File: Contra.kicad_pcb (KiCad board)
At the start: 2 copper layers, 251.5 x 76.2 mm, 152 parts, among them J1 Conn_01x03, J2 Conn_01x02, SW1 SW_PUSH, SW2 SW_SPDT, U1 ProMicro

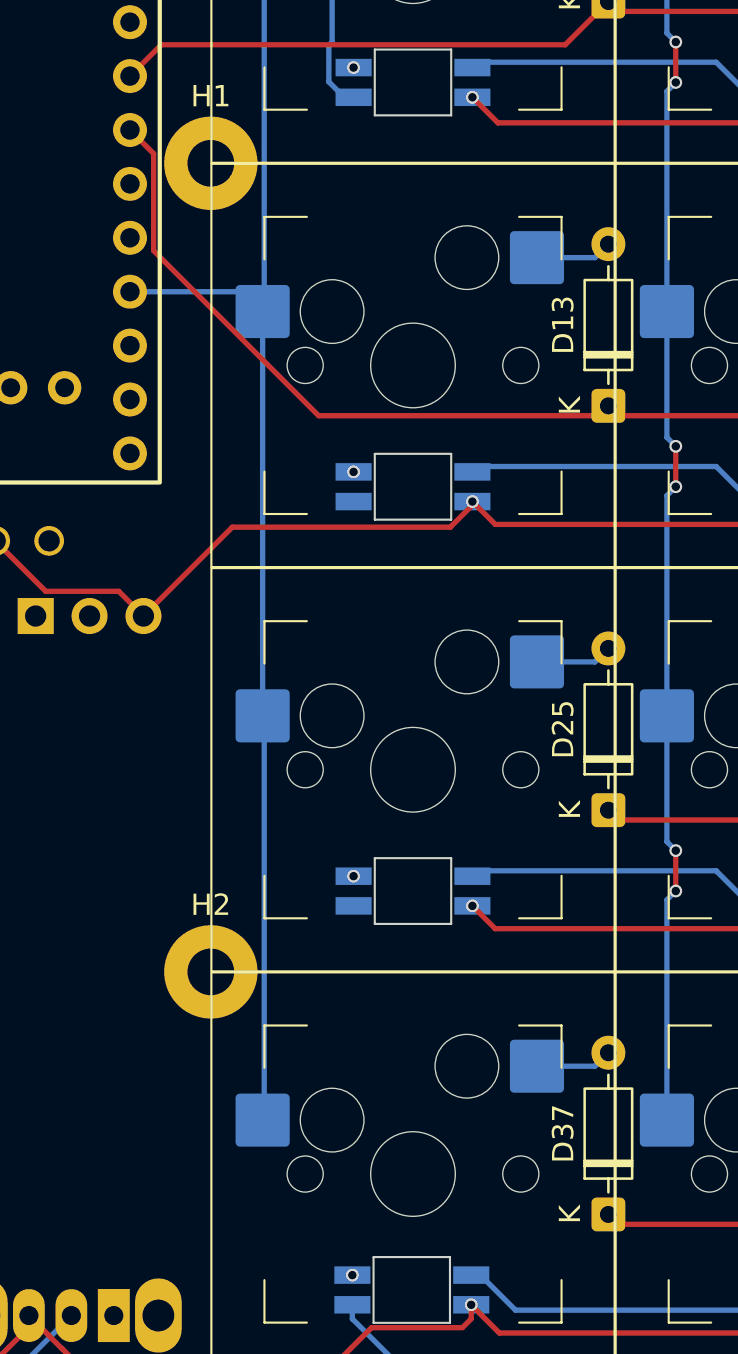
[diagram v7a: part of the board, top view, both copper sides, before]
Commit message: connect rows to mcu
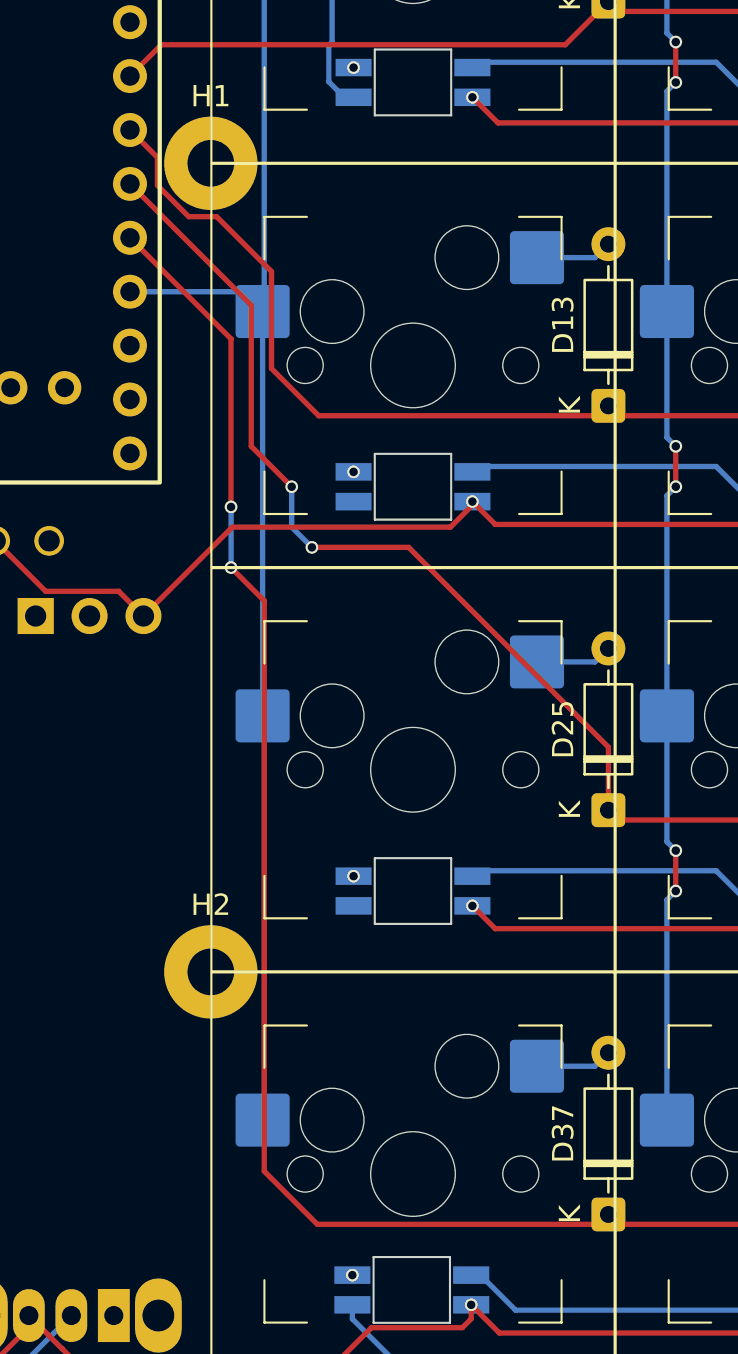
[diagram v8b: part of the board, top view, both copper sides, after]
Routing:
- net ROW3: track 200.3 -> 263.7 mm, vias 0 -> 2
- net ROW2: track 199.3 -> 240.9 mm, vias 0 -> 2
- net ROW1: track 229.7 -> 230.4 mm
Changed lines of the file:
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@@
+	)
+	(segment
+		(start 42.2525 70.210521)
+		(end 40.95751 68.915531)
+		(width 0.25)
+		(layer "F.Cu")
+		(net "ROW1")
+	)
+	(segment
+		(start 43.725752 73)
+		(end 42.2525 71.526748)
+		(width 0.25)
+		(layer "F.Cu")
+		(net "ROW1")
+	)
+	(segment
+		(start 49.847716 82.3789)
+		(end 47.625 80.156184)
+		(width 0.25)
+		(layer "F.Cu")
+		(net "ROW1")
 	)
 	(segment
@@
 	)
 	(segment
-		(start 42.07251 74.603694)
-		(end 42.07251 70.030531)
-		(width 0.25)
-		(layer "F.Cu")
-		(net "ROW1")
-	)
-	(segment
 		(start 159.2139 82.3789)
 		(end 177.3361 82.3789)
@@
 	)
 	(segment
+		(start 42.2525 71.526748)
+		(end 42.2525 70.210521)
+		(width 0.25)
+		(layer "F.Cu")
+		(net "ROW1")
+	)
+	(segment
+		(start 197.3139 82.3789)
+		(end 215.4361 82.3789)
+		(width 0.25)
+		(layer "F.Cu")
+		(net "ROW1")
+	)
+	(segment
+		(start 47.625 80.156184)
+		(end 47.625 75.583021)
+		(width 0.25)
+		(layer "F.Cu")
+		(net "ROW1")
+	)
+	(segment
+		(start 121.1139 82.3789)
+		(end 139.2361 82.3789)
+		(width 0.25)
+		(layer "F.Cu")
+		(net "ROW1")
+	)
+	(segment
+		(start 45.041979 73)
+		(end 43.725752 73)
+		(width 0.25)
+		(layer "F.Cu")
+		(net "ROW1")
+	)
+	(segment
 		(start 63.0361 82.3789)
 		(end 49.847716 82.3789)
@@
 	)
 	(segment
-		(start 197.3139 82.3789)
-		(end 215.4361 82.3789)
-		(width 0.25)
-		(layer "F.Cu")
-		(net "ROW1")
-	)
-	(segment
-		(start 121.1139 82.3789)
-		(end 139.2361 82.3789)
-		(width 0.25)
-		(layer "F.Cu")
-		(net "ROW1")
-	)
-	(segment
-		(start 49.847716 82.3789)
-		(end 42.07251 74.603694)
-		(width 0.25)
-		(layer "F.Cu")
-		(net "ROW1")
-	)
-	(segment
 		(start 235.4139 82.3789)
 		(end 253.5361 82.3789)
@@
 	)
 	(segment
-		(start 42.07251 70.030531)
-		(end 40.95751 68.915531)
-		(width 0.25)
-		(layer "F.Cu")
-		(net "ROW1")
-	)
-	(segment
 		(start 140.1639 82.3789)
 		(end 158.2861 82.3789)
@@
 	)
 	(segment
+		(start 47.625 75.583021)
+		(end 45.041979 73)
+		(width 0.25)
+		(layer "F.Cu")
+		(net "ROW1")
+	)
+	(segment
 		(start 62.865 74.93)
 		(end 63.5 74.295)
@@
 	)
 	(segment
+		(start 63.5 97.99585)
+		(end 54.08665 88.5825)
+		(width 0.25)
+		(layer "F.Cu")
+		(net "ROW2")
+	)
+	(segment
+		(start 46.6725 83.82)
+		(end 46.6725 77.170521)
+		(width 0.25)
+		(layer "F.Cu")
+		(net "ROW2")
+	)
+	(segment
 		(start 139.2361 101.4289)
 		(end 121.1139 101.4289)
@@
 	)
 	(segment
+		(start 48.5775 85.725)
+		(end 46.6725 83.82)
+		(width 0.25)
+		(layer "F.Cu")
+		(net "ROW2")
+	)
+	(segment
+		(start 46.6725 77.170521)
+		(end 40.95751 71.455531)
+		(width 0.25)
+		(layer "F.Cu")
+		(net "ROW2")
+	)
+	(segment
+		(start 63.5 100.965)
+		(end 63.5 97.99585)
+		(width 0.25)
+		(layer "F.Cu")
+		(net "ROW2")
+	)
+	(segment
 		(start 120.1861 101.4289)
 		(end 102.0639 101.4289)
@@
 	)
 	(segment
+		(start 54.08665 88.5825)
+		(end 49.53 88.5825)
+		(width 0.25)
+		(layer "F.Cu")
+		(net "ROW2")
+	)
+	(segment
 		(start 253.5361 101.4289)
 		(end 235.4139 101.4289)
@@
 		(net "ROW2")
 	)
+	(via
+		(at 49.53 88.5825)
+		(size 0.6)
+		(drill 0.4)
+		(layers "F.Cu" "B.Cu")
+		(net "ROW2")
+	)
+	(via
+		(at 48.5775 85.725)
+		(size 0.6)
+		(drill 0.4)
+		(layers "F.Cu" "B.Cu")
+		(net "ROW2")
+	)
+	(segment
+		(start 49.53 88.5825)
+		(end 48.5775 87.63)
+		(width 0.25)
+		(layer "B.Cu")
+		(net "ROW2")
+	)
+	(segment
+		(start 48.5775 87.63)
+		(end 48.5775 85.725)
+		(width 0.25)
+		(layer "B.Cu")
+		(net "ROW2")
+	)
 	(segment
 		(start 62.865 93.98)
@@
 	)
 	(segment
+		(start 47.2825 117.9775)
+		(end 47.2825 91.0975)
+		(width 0.25)
+		(layer "F.Cu")
+		(net "ROW3")
+	)
+	(segment
 		(start 197.3139 120.4789)
 		(end 215.4361 120.4789)
@@
 	)
 	(segment
+		(start 45.72 78.758021)
+		(end 40.95751 73.995531)
+		(width 0.25)
+		(layer "F.Cu")
+		(net "ROW3")
+	)
+	(segment
+		(start 45.72 86.6775)
+		(end 45.72 78.758021)
+		(width 0.25)
+		(layer "F.Cu")
+		(net "ROW3")
+	)
+	(segment
 		(start 178.2639 120.4789)
 		(end 196.3861 120.4789)
@@
 	)
 	(segment
+		(start 49.7839 120.4789)
+		(end 47.2825 117.9775)
+		(width 0.25)
+		(layer "F.Cu")
+		(net "ROW3")
+	)
+	(segment
 		(start 83.0139 120.4789)
 		(end 101.1361 120.4789)
@@
 	)
 	(segment
+		(start 63.0361 120.4789)
+		(end 49.7839 120.4789)
+		(width 0.25)
+		(layer "F.Cu")
+		(net "ROW3")
+	)
+	(segment
+		(start 47.2825 91.0975)
+		(end 45.72 89.535)
+		(width 0.25)
+		(layer "F.Cu")
+		(net "ROW3")
+	)
+	(segment
 		(start 235.4139 120.4789)
 		(end 253.5361 120.4789)
@@
 		(net "ROW3")
 	)
+	(via
+		(at 45.72 89.535)
+		(size 0.6)
+		(drill 0.4)
+		(layers "F.Cu" "B.Cu")
+		(net "ROW3")
+	)
+	(via
+		(at 45.72 86.6775)
+		(size 0.6)
+		(drill 0.4)
+		(layers "F.Cu" "B.Cu")
+		(net "ROW3")
+	)
+	(segment
+		(start 45.72 89.535)
+		(end 45.72 86.6775)
+		(width 0.25)
+		(layer "B.Cu")
+		(net "ROW3")
+	)
